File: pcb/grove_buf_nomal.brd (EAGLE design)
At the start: 31.9 x 10.2 mm, 2 parts, among them J1 4P-2.0-90D, J2 4P-2.0-90D

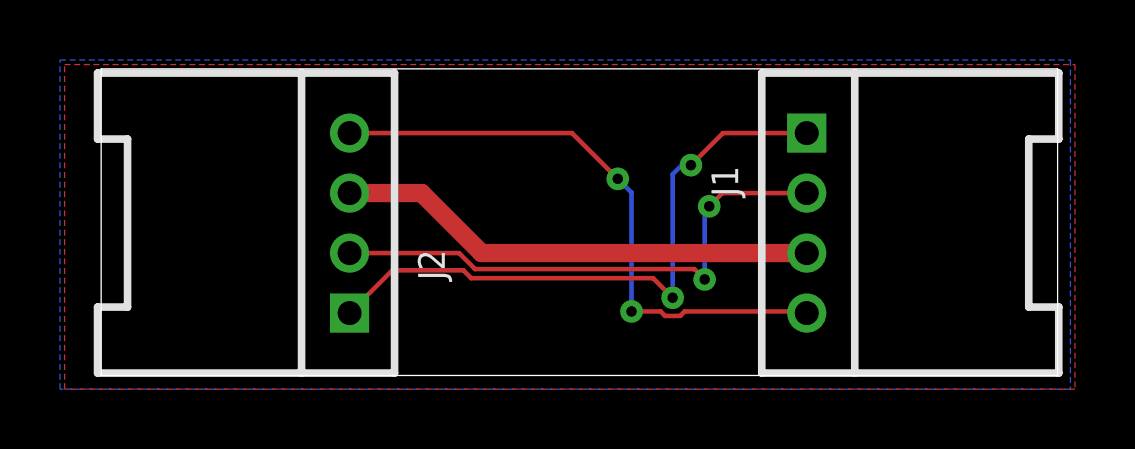
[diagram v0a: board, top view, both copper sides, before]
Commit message: Update grove_buf_nomal.brd
シルク修正および基板サイズ変更
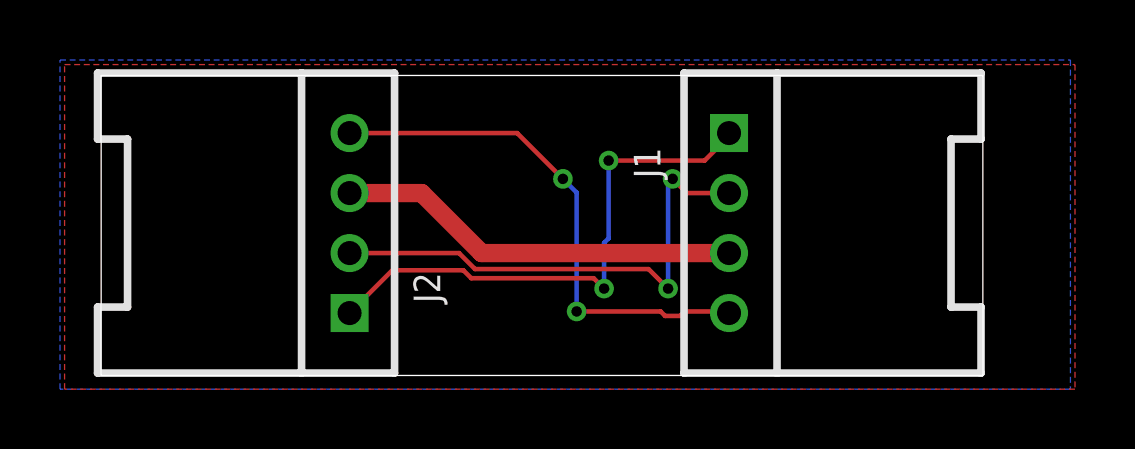
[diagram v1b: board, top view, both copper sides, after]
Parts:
- moved J1 2.59 mm to (21.5, 5.08)
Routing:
- net 1: track 20.9 -> 18.1 mm
- net VCC: track 16.1 -> 13.5 mm
- net GND: track 20.2 -> 17.6 mm
- net 2: track 18.1 -> 16.9 mm
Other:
- board size 31.9 x 10.2 mm -> 29.4 x 10 mm
- board text added: "Repeater"
- board text removed: "Repeter"

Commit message: サイズを30mmピッタリに微修正
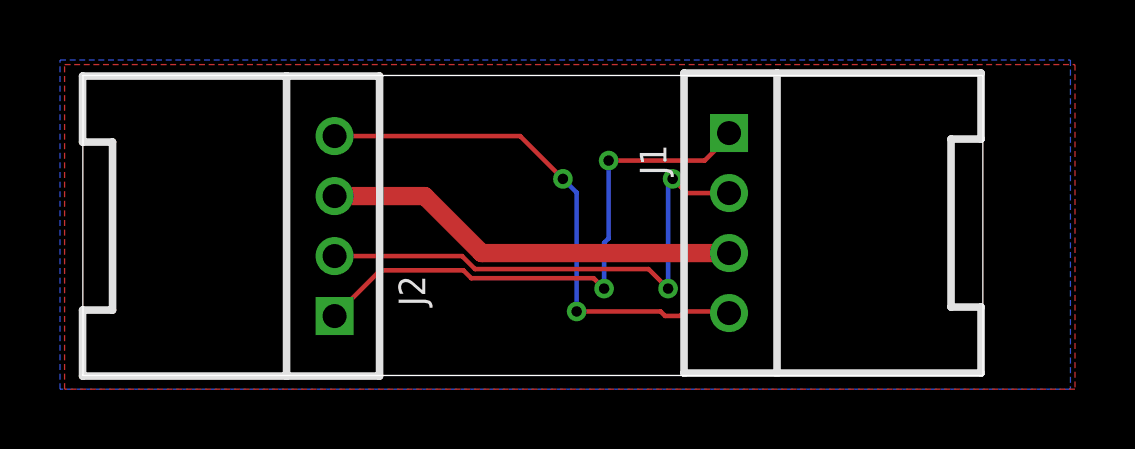
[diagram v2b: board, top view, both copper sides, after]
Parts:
- moved J2 0.51 mm to (8.39, 4.98)
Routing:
- net 1: track 18.1 -> 18.7 mm
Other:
- board size 29.4 x 10 mm -> 30 x 10 mm
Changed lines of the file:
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@@
 <setting verticaltext="up"/>
 </settings>
-<grid distance="6" unitdist="mil" unit="mm" style="lines" multiple="1" display="yes" altdistance="5" altunitdist="mil" altunit="mil"/>
+<grid distance="0.1" unitdist="mm" unit="mm" style="lines" multiple="1" display="yes" altdistance="5" altunitdist="mil" altunit="mil"/>
 <layers>
 <layer number="1" name="Top" color="4" fill="1" visible="yes" active="yes"/>
@@
 <board>
 <plain>
-<wire x1="0.6096" y1="0" x2="30" y2="0" width="0" layer="20"/>
+<wire x1="0" y1="0" x2="30" y2="0" width="0" layer="20"/>
 <wire x1="30" y1="0" x2="30" y2="10" width="0" layer="20"/>
-<wire x1="30" y1="10" x2="0.6096" y2="10" width="0" layer="20"/>
-<wire x1="0.6096" y1="10" x2="0.6096" y2="0" width="0" layer="20"/>
-<text x="18.7452" y="8.382" size="1.27" layer="26" rot="MR0">Repeater</text>
-<text x="7.9248" y="1.8288" size="0.8128" layer="26" rot="MR0">pin2</text>
-<text x="7.9248" y="3.81" size="0.8128" layer="26" rot="MR0">pin1</text>
-<text x="7.9248" y="5.6388" size="0.8128" layer="26" rot="MR0">VDD</text>
-<text x="7.9248" y="7.7724" size="0.8128" layer="26" rot="MR0">GND</text>
+<wire x1="30" y1="10" x2="0" y2="10" width="0" layer="20"/>
+<wire x1="0" y1="10" x2="0" y2="0" width="0" layer="20"/>
+<text x="18.5452" y="8.382" size="1.27" layer="26" rot="MR0">Repeater</text>
+<text x="7.3248" y="1.6288" size="0.8128" layer="26" rot="MR0">pin2</text>
+<text x="7.3248" y="3.61" size="0.8128" layer="26" rot="MR0">pin1</text>
+<text x="7.3248" y="5.6388" size="0.8128" layer="26" rot="MR0">VDD</text>
+<text x="7.2248" y="7.6724" size="0.8128" layer="26" rot="MR0">GND</text>
 <text x="24.9936" y="7.7724" size="0.8128" layer="26" rot="MR0">pin2</text>
 <text x="24.9936" y="5.7912" size="0.8128" layer="26" rot="MR0">pin1</text>
 <text x="24.9936" y="3.6576" size="0.8128" layer="26" rot="MR0">VDD</text>
-<text x="24.9936" y="1.8288" size="0.8128" layer="26" rot="MR0">GND</text>
+<text x="25.0936" y="1.6288" size="0.8128" layer="26" rot="MR0">GND</text>
 <polygon width="0.1524" layer="26">
-<vertex x="19.812" y="3.9624"/>
-<vertex x="19.812" y="5.9436"/>
-<vertex x="12.8016" y="5.9436"/>
-<vertex x="12.8016" y="7.0104"/>
-<vertex x="10.4625375" y="4.808928125"/>
-<vertex x="12.8016" y="2.76225"/>
-<vertex x="12.8016" y="3.9624"/>
+<vertex x="19.612" y="4.0624"/>
+<vertex x="19.612" y="6.0436"/>
+<vertex x="12.6016" y="6.0436"/>
+<vertex x="12.6016" y="7.1104"/>
+<vertex x="10.2625375" y="4.908928125"/>
+<vertex x="12.6016" y="2.86225"/>
+<vertex x="12.6016" y="4.0624"/>
 </polygon>
-<text x="18.7452" y="0.762" size="0.8128" layer="26" rot="MR0">@hirowo556</text>
+<text x="18.3452" y="0.762" size="0.8128" layer="26" rot="MR0">@hirowo556</text>
 </plain>
 <attributes>
@@
 <elements>
 <element name="J1" library="Seeed-Connector" package="HW4-2.0-90D" value="4P-2.0-90D" x="21.5392" y="5.08" smashed="yes" rot="R270">
-<attribute name="NAME" x="18.3642" y="7.5946" size="0.889" layer="25" font="vector" ratio="11" rot="R270"/>
+<attribute name="NAME" x="18.5642" y="7.6946" size="0.889" layer="25" font="vector" ratio="11" rot="R270"/>
 </element>
-<element name="J2" library="Seeed-Connector" package="HW4-2.0-90D" value="4P-2.0-90D" x="8.89" y="5.08" smashed="yes" rot="R90">
-<attribute name="NAME" x="11.9126" y="2.413" size="0.889" layer="25" font="vector" ratio="11" rot="R90"/>
+<element name="J2" library="Seeed-Connector" package="HW4-2.0-90D" value="4P-2.0-90D" x="8.39" y="4.98" smashed="yes" rot="R90">
+<attribute name="NAME" x="11.4126" y="2.313" size="0.889" layer="25" font="vector" ratio="11" rot="R90"/>
 </element>
 </elements>
@@
 <contactref element="J1" pad="3"/>
 <contactref element="J2" pad="3"/>
-<wire x1="8.89" y1="6.08" x2="11.2936" y2="6.08" width="0.6096" layer="1"/>
+<wire x1="8.39" y1="5.98" x2="11.3936" y2="5.98" width="0.6096" layer="1"/>
 <wire x1="13.2936" y1="4.08" x2="21.5392" y2="4.08" width="0.6096" layer="1"/>
-<wire x1="11.2936" y1="6.08" x2="13.2936" y2="4.08" width="0.6096" layer="1"/>
+<wire x1="11.3936" y1="5.98" x2="13.2936" y2="4.08" width="0.6096" layer="1"/>
 </signal>
 <signal name="GND">
 <contactref element="J1" pad="4"/>
 <contactref element="J2" pad="4"/>
-<wire x1="8.89" y1="8.08" x2="14.4752" y2="8.08" width="0.1524" layer="1"/>
-<wire x1="14.4752" y1="8.08" x2="16.002" y2="6.5532" width="0.1524" layer="1"/>
+<wire x1="8.39" y1="7.98" x2="14.5752" y2="7.98" width="0.1524" layer="1"/>
+<wire x1="14.5752" y1="7.98" x2="16.002" y2="6.5532" width="0.1524" layer="1"/>
 <via x="16.002" y="6.5532" extent="1-16" drill="0.35"/>
 <wire x1="16.002" y1="6.5532" x2="16.4592" y2="6.096" width="0.1524" layer="16"/>
@@
 <contactref element="J1" pad="1"/>
 <contactref element="J2" pad="1"/>
-<wire x1="8.89" y1="2.08" x2="10.3152" y2="3.5052" width="0.1524" layer="1"/>
-<wire x1="10.3152" y1="3.5052" x2="12.683" y2="3.5052" width="0.1524" layer="1"/>
+<wire x1="8.39" y1="1.98" x2="9.9152" y2="3.5052" width="0.1524" layer="1"/>
+<wire x1="9.9152" y1="3.5052" x2="12.683" y2="3.5052" width="0.1524" layer="1"/>
 <wire x1="12.683" y1="3.5052" x2="12.9464" y2="3.2418" width="0.1524" layer="1"/>
 <wire x1="17.0274" y1="3.2418" x2="17.3736" y2="2.8956" width="0.1524" layer="1"/>
@@
 <contactref element="J1" pad="2"/>
 <contactref element="J2" pad="2"/>
-<wire x1="8.89" y1="4.08" x2="12.53925625" y2="4.08" width="0.1524" layer="1"/>
-<wire x1="12.53925625" y1="4.08" x2="13.07265625" y2="3.5466" width="0.1524" layer="1"/>
+<wire x1="8.39" y1="3.98" x2="12.63925625" y2="3.98" width="0.1524" layer="1"/>
+<wire x1="12.63925625" y1="3.98" x2="13.07265625" y2="3.5466" width="0.1524" layer="1"/>
 <wire x1="18.8562" y1="3.5466" x2="19.5072" y2="2.8956" width="0.1524" layer="1"/>
 <wire x1="13.07265625" y1="3.5466" x2="18.8562" y2="3.5466" width="0.1524" layer="1"/>
